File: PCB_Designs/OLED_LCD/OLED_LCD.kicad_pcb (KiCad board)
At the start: 2 copper layers, 25 parts, among them P1 CONN_01X10, P2 CONN_01X20, SW1 Rotary_Encoder_Switch, U1 MCP23017, U2 MCP23017, U3 CHERRY-MX

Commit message: s¨å
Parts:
- removed 0.1k1: 100, Resistors_SMD:R_0603_HandSoldering
- moved 100n3 88.0 mm to (178.8, 84.1)
- moved R4 72.7 mm to (116.6, 117.6)
- moved 10k8 65.3 mm to (139.2, 97.0), turned to 180 degrees
- moved 100n4 61.6 mm to (112.3, 106.4)
- moved 10k3 58.6 mm to (105.4, 87.1), turned to 90 degrees
- moved 10k1 57.5 mm to (100.3, 87.1)
- moved 10k2 53.8 mm to (113.3, 95.5)
- moved R2 53.1 mm to (102.6, 127.5)
- moved R1 50.1 mm to (112.0, 117.6), turned to 180 degrees
- moved 100n2 47.5 mm to (119.4, 91.4), turned to 180 degrees
- moved C1 45.3 mm to (112.0, 120.1), turned to 180 degrees
- moved 10k4 42.7 mm to (113.3, 91.4), turned to 180 degrees
- moved P1 41.0 mm to (129.3, 135.9)
- moved 10k7 40.9 mm to (137.7, 108.7), turned to 90 degrees
- moved R3 40.7 mm to (112.0, 115.1)
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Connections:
- P2 pad 19: /LED+ -> /LCD_BACKLIGHT
- U1 pad 18: /RST# -> Net-(U1-Pad18)
- U2 pad 18: /RST# -> Net-(U2-Pad18)
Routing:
- net /VCC5: track 0.00 -> 363.4 mm, vias 0 -> 2
- net GND: track 0.00 -> 215.9 mm, vias 0 -> 14
- net /LCD_BACKLIGHT: track 0.00 -> 76.9 mm, vias 0 -> 4
- net /CS2: track 0.00 -> 72.5 mm
- net /SCL#: track 0.00 -> 63.1 mm
- net /V0: track 0.00 -> 62.2 mm
- net /RS: track 0.00 -> 61.9 mm
- net /RST: track 0.00 -> 59.9 mm, vias 0 -> 2
- net /RW: track 0.00 -> 57.3 mm
- net /E: track 0.33 -> 53.1 mm
- net /SDA#: track 0.15 -> 50.5 mm
- net /INTA: track 0.00 -> 30.1 mm
- net /ENCODERA: track 0.00 -> 27.6 mm
- net /D0: track 0.00 -> 25.0 mm
- net /D1: track 0.00 -> 24.5 mm
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- added copper zone on F.Cu, net GND
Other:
- net class Default: clearance 0.6 -> 0.5
- rule trace_clearance: 0.6 -> 0.5

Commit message: LCD123
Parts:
- P1: footprint Connectors:IDC_Header_Straight_10pins -> Connectors_Multicomp:Multicomp_MC9A22-1034_2x05x2.54mm_Angled; moved to B.Cu
- moved P1 30.9 mm to (98.6, 133.1), turned to 0 degrees
- moved 100n2 1.60 mm to (117.8, 91.4)
- moved 100n1 1.44 mm to (113.3, 97.4)
- moved 10k5 0.74 mm to (112.3, 104.6)
- moved C1 0.71 mm to (112.0, 119.4)
- moved R3 0.66 mm to (112.0, 115.7)
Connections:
- net /INTB renamed Net-(U1-Pad19)
- P1 pad 10: Net-(P1-Pad10) -> /INTA
- P1 pad 4: Net-(P1-Pad4) -> GND
- P1 pad 6: Net-(P1-Pad6) -> /SDA#
- P1 pad 8: Net-(P1-Pad8) -> /SCL#
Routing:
- net /VCC5: track 363.4 -> 281.7 mm, vias 2 -> 4
- net /SDA#: track 50.5 -> 72.6 mm
- net /LCD_BACKLIGHT: track 76.9 -> 94.4 mm, vias 4 -> 2
- net /SCL#: track 63.1 -> 79.5 mm
- net GND: track 215.9 -> 201.1 mm, vias 14 -> 10
- net /INTA: track 30.1 -> 37.7 mm
- net Net-(C1-Pad1): track 7.51 -> 6.14 mm
- net /ENCODERA: track 27.6 -> 26.6 mm
- net Net-(10k1-Pad2): track 17.9 -> 17.0 mm
- net /ENCODERSW: track 24.5 -> 23.7 mm
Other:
- board text added: "Sunshine"

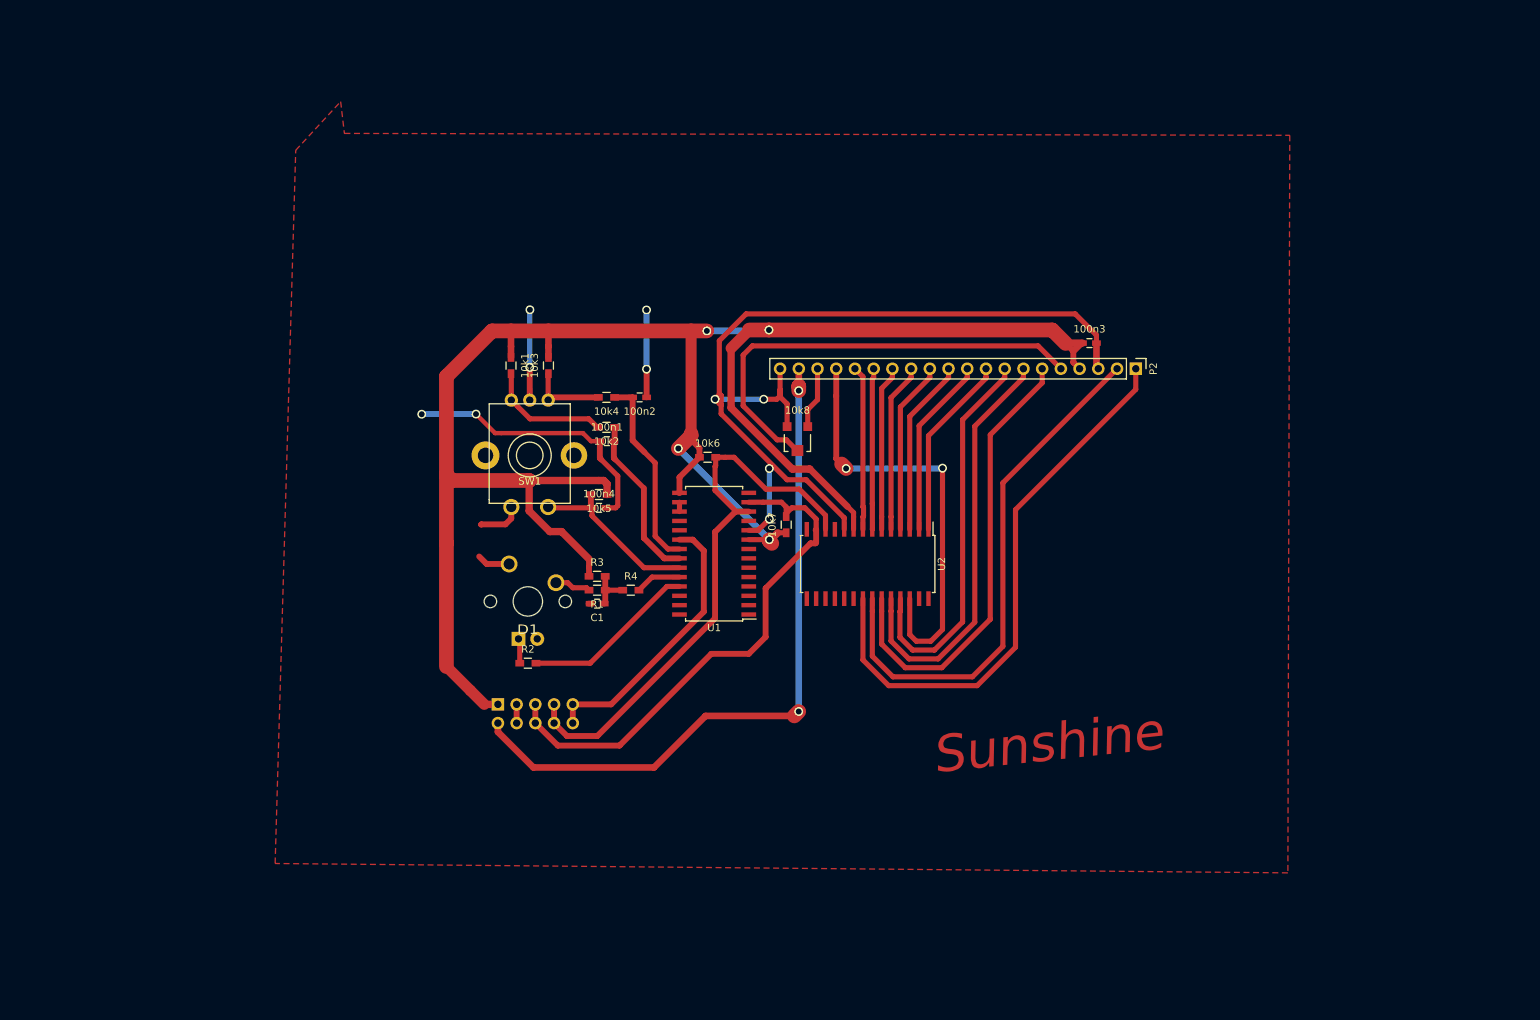
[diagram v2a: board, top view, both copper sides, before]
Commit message: Completed OLED_LCD_PCB v1.1
* Added Mountingholes.
* Added "Fatpads" for vias (were on some but not all earlier)
* Added bottom ground (Or etching will be a bitch)
* Added Edge cuts (105x65mm)
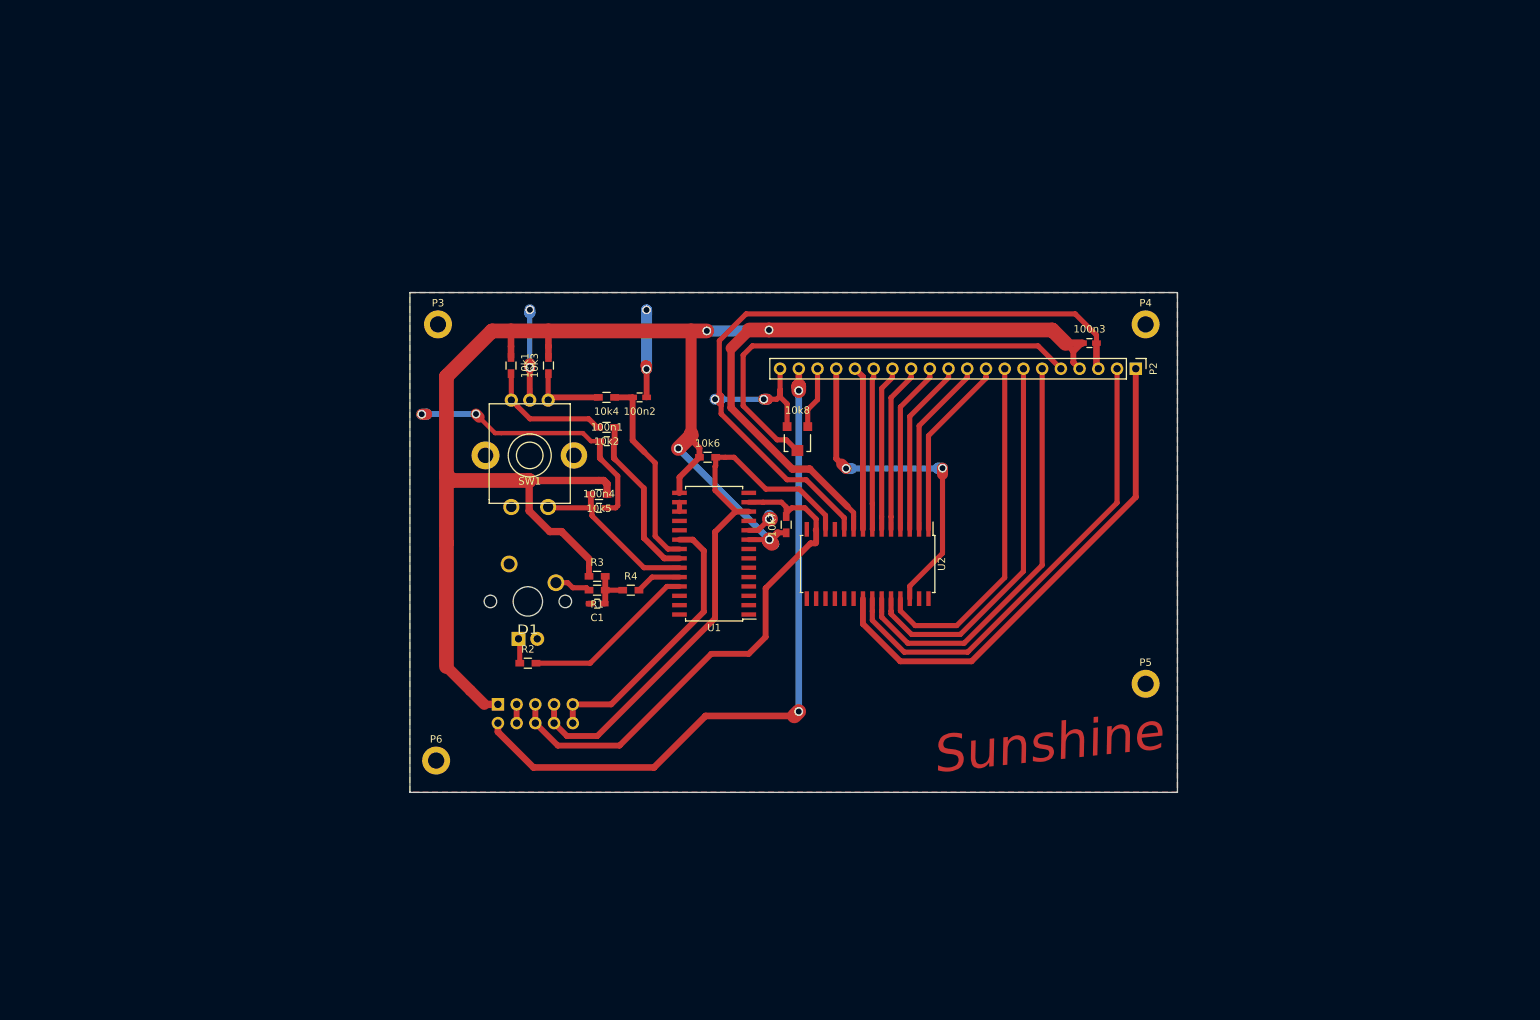
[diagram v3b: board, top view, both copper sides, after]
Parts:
- added P3: CONN_01X01, Mounting_Holes:MountingHole_2.2mm_M2_DIN965_Pad, F.Cu at (90.4, 81.5)
- added P4: CONN_01X01, Mounting_Holes:MountingHole_2.2mm_M2_DIN965_Pad, F.Cu at (186.4, 81.5)
- added P5: CONN_01X01, Mounting_Holes:MountingHole_2.2mm_M2_DIN965_Pad, F.Cu at (186.4, 130.3)
- added P6: CONN_01X01, Mounting_Holes:MountingHole_2.2mm_M2_DIN965_Pad, F.Cu at (90.2, 140.7)
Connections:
- U1 pad 1: Net-(U1-Pad1) -> (no net)
- U1 pad 18: Net-(U1-Pad18) -> (no net)
- U1 pad 19: Net-(U1-Pad19) -> (no net)
- U1 pad 2: Net-(U1-Pad2) -> (no net)
- U1 pad 26: Net-(U1-Pad26) -> (no net)
- U1 pad 27: Net-(U1-Pad27) -> (no net)
- U1 pad 28: Net-(U1-Pad28) -> (no net)
- U1 pad 3: Net-(U1-Pad3) -> (no net)
- U1 pad 4: Net-(U1-Pad4) -> (no net)
- U1 pad 5: Net-(U1-Pad5) -> (no net)
- U1 pad 6: Net-(U1-Pad6) -> (no net)
- U1 pad 7: Net-(U1-Pad7) -> (no net)
- U1 pad 8: Net-(U1-Pad8) -> (no net)
- U2 pad 18: Net-(U2-Pad18) -> (no net)
- U2 pad 19: Net-(U2-Pad19) -> (no net)
- U2 pad 20: Net-(U2-Pad20) -> (no net)
- U2 pad 27: Net-(U2-Pad27) -> (no net)
- U2 pad 28: Net-(U2-Pad28) -> (no net)
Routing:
- net /RST: track 59.5 -> 48.2 mm
- net GND: track 201.1 -> 191.6 mm, vias 10 -> 9
- net /CS1: track 77.2 -> 69.2 mm
- net /CS2: track 72.5 -> 64.5 mm
- net /E: track 53.1 -> 48.0 mm
- net /RS: track 61.9 -> 56.8 mm
- net /RW: track 57.3 -> 52.2 mm
- net /VCC5: track 281.7 -> 283.3 mm
- net /LCD_BACKLIGHT: track 94.4 -> 95.0 mm
- added copper zone on B.Cu, net GND
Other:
- board outline added: 104.1 x 67.8 mm

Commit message: hej
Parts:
- removed 10k8: 10k, Potentiometers:Potentiometer_Trimmer-EVM3E
- P2: value CONN_01X20 -> CONN_01X16; footprint Pin_Headers:Pin_Header_Straight_1x20_Pitch2.54mm -> Pin_Headers:Pin_Header_Straight_1x16_Pitch2.54mm
- moved 100n3 2.03 mm to (180.8, 83.5)
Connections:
- P2 pad 1: /CS1 -> GND
- P2 pad 10: /D1 -> /D3
- P2 pad 11: /D2 -> /D4
- P2 pad 12: /D3 -> /D5
- P2 pad 13: /D4 -> /D6
- P2 pad 14: /D5 -> /D7
- P2 pad 15: /D6 -> /LCD_BACKLIGHT
- P2 pad 16: /D7 -> GND
- P2 pad 2: /CS2 -> /VCC5
- P2 pad 3: GND -> Net-(P2-Pad3)
- P2 pad 4: /VCC5 -> /RS
- P2 pad 5: /V0 -> /RW
- P2 pad 6: /RS -> /E
- P2 pad 7: /RW -> /D0
- P2 pad 8: /E -> /D1
- P2 pad 9: /D0 -> /D2
- P3 pad 1: (no net) -> Net-(P3-Pad1)
- P4 pad 1: (no net) -> Net-(P4-Pad1)
- P5 pad 1: (no net) -> Net-(P5-Pad1)
- P6 pad 1: (no net) -> Net-(P6-Pad1)
- U1 pad 1: (no net) -> Net-(U1-Pad1)
- U1 pad 18: (no net) -> Net-(U1-Pad18)
- U1 pad 19: (no net) -> Net-(U1-Pad19)
- U1 pad 2: (no net) -> Net-(U1-Pad2)
- U1 pad 26: (no net) -> Net-(U1-Pad26)
- U1 pad 27: (no net) -> Net-(U1-Pad27)
- U1 pad 28: (no net) -> Net-(U1-Pad28)
- U1 pad 3: (no net) -> Net-(U1-Pad3)
- U1 pad 4: (no net) -> Net-(U1-Pad4)
- U1 pad 5: (no net) -> Net-(U1-Pad5)
- U1 pad 6: (no net) -> Net-(U1-Pad6)
- U1 pad 7: (no net) -> Net-(U1-Pad7)
- U1 pad 8: (no net) -> Net-(U1-Pad8)
- U2 pad 18: (no net) -> Net-(U2-Pad18)
- U2 pad 19: (no net) -> Net-(U2-Pad19)
- U2 pad 20: (no net) -> Net-(U2-Pad20)
- U2 pad 21: /CS1 -> Net-(U2-Pad21)
- U2 pad 22: /CS2 -> Net-(U2-Pad22)
- U2 pad 26: /RST -> Net-(U2-Pad26)
- U2 pad 27: (no net) -> Net-(U2-Pad27)
- U2 pad 28: (no net) -> Net-(U2-Pad28)
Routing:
- net /CS1: track 69.2 -> 0.00 mm
- net /CS2: track 64.5 -> 0.00 mm
- net /V0: track 61.7 -> 0.00 mm
- net /RST: track 48.2 -> 0.00 mm, vias 2 -> 0
- net /VEE: track 8.40 -> 0.00 mm
- net /VCC5: track 283.3 -> 288.5 mm, vias 4 -> 2
- net /D1: track 24.5 -> 26.9 mm
- net /D6: track 21.9 -> 24.0 mm
- net /D5: track 22.4 -> 24.5 mm
- net /D4: track 22.9 -> 25.0 mm
- net /D2: track 24.0 -> 26.1 mm
- net /D3: track 23.5 -> 25.6 mm
- net /D0: track 25.0 -> 27.1 mm
- net /LCD_BACKLIGHT: track 95.0 -> 93.2 mm
- net /E: track 48.0 -> 46.5 mm
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
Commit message: stuff
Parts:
- moved P5 10.6 mm to (186.4, 140.9)
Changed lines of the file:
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@@
-(kicad_pcb (version 4) (host pcbnew 4.0.5)
+(kicad_pcb (version 4) (host pcbnew 4.0.4-stable)
   (general
     (links 70)
@@
   )
   (setup
-    (last_trace_width 1.5)
+    (last_trace_width 0.8)
     (user_trace_width 0.6)
     (user_trace_width 0.7)
@@
   )
   (module Mounting_Holes:MountingHole_2.2mm_M2_DIN965_Pad (layer F.Cu)
-    (at 186.436 130.302)
+    (at 186.42 140.92)
     (descr "Mounting Hole 2.2mm, M2, DIN965")
     (tags "mounting hole 2.2mm m2 din965")

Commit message: LCD Reset -> 5V
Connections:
- U1 pad 18: Net-(U1-Pad18) -> /VCC5
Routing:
- net /VCC5: track 288.5 -> 297.7 mm
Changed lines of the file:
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@@
 (kicad_pcb (version 4) (host pcbnew 4.0.4-stable)
   (general
-    (links 70)
-    (no_connects 0)
-    (area 68.62 64.305136 212.368541 149.471)
+    (links 71)
+    (no_connects 1)
+    (area 86.538999 77.140999 190.829001 145.109001)
     (thickness 1.6)
     (drawings 10)
-    (tracks 310)
+    (tracks 315)
     (zones 0)
     (modules 27)
-    (nets 54)
+    (nets 53)
   )
   (page A4)
@@
   (net 39 "Net-(U1-Pad7)")
   (net 40 "Net-(U1-Pad8)")
-  (net 41 "Net-(U1-Pad18)")
-  (net 42 "Net-(U1-Pad19)")
-  (net 43 "Net-(U1-Pad26)")
-  (net 44 "Net-(U1-Pad27)")
-  (net 45 "Net-(U1-Pad28)")
-  (net 46 "Net-(U2-Pad18)")
-  (net 47 "Net-(U2-Pad19)")
-  (net 48 "Net-(U2-Pad20)")
-  (net 49 "Net-(U2-Pad21)")
-  (net 50 "Net-(U2-Pad22)")
-  (net 51 "Net-(U2-Pad26)")
-  (net 52 "Net-(U2-Pad27)")
-  (net 53 "Net-(U2-Pad28)")
+  (net 41 "Net-(U1-Pad19)")
+  (net 42 "Net-(U1-Pad26)")
+  (net 43 "Net-(U1-Pad27)")
+  (net 44 "Net-(U1-Pad28)")
+  (net 45 "Net-(U2-Pad18)")
+  (net 46 "Net-(U2-Pad19)")
+  (net 47 "Net-(U2-Pad20)")
+  (net 48 "Net-(U2-Pad21)")
+  (net 49 "Net-(U2-Pad22)")
+  (net 50 "Net-(U2-Pad26)")
+  (net 51 "Net-(U2-Pad27)")
+  (net 52 "Net-(U2-Pad28)")
   (net_class Default "This is the default net class."
     (clearance 0.5)
@@
     (add_net "Net-(R1-Pad2)")
     (add_net "Net-(U1-Pad1)")
-    (add_net "Net-(U1-Pad18)")
     (add_net "Net-(U1-Pad19)")
     (add_net "Net-(U1-Pad2)")
@@
       (net 9 GND))
     (pad 18 smd rect (at 4.7 4.445 270) (size 2 0.6) (layers F.Cu F.Paste F.Mask)
-      (net 46 "Net-(U2-Pad18)"))
+      (net 45 "Net-(U2-Pad18)"))
     (pad 19 smd rect (at 4.7 3.175 270) (size 2 0.6) (layers F.Cu F.Paste F.Mask)
-      (net 47 "Net-(U2-Pad19)"))
+      (net 46 "Net-(U2-Pad19)"))
     (pad 20 smd rect (at 4.7 1.905 270) (size 2 0.6) (layers F.Cu F.Paste F.Mask)
-      (net 48 "Net-(U2-Pad20)"))
+      (net 47 "Net-(U2-Pad20)"))
     (pad 21 smd rect (at 4.7 0.635 270) (size 2 0.6) (layers F.Cu F.Paste F.Mask)
-      (net 49 "Net-(U2-Pad21)"))
+      (net 48 "Net-(U2-Pad21)"))
     (pad 22 smd rect (at 4.7 -0.635 270) (size 2 0.6) (layers F.Cu F.Paste F.Mask)
-      (net 50 "Net-(U2-Pad22)"))
+      (net 49 "Net-(U2-Pad22)"))
     (pad 23 smd rect (at 4.7 -1.905 270) (size 2 0.6) (layers F.Cu F.Paste F.Mask)
       (net 10 /RS))
@@
       (net 12 /E))
     (pad 26 smd rect (at 4.7 -5.715 270) (size 2 0.6) (layers F.Cu F.Paste F.Mask)
-      (net 51 "Net-(U2-Pad26)"))
+      (net 50 "Net-(U2-Pad26)"))
     (pad 27 smd rect (at 4.7 -6.985 270) (size 2 0.6) (layers F.Cu F.Paste F.Mask)
-      (net 52 "Net-(U2-Pad27)"))
+      (net 51 "Net-(U2-Pad27)"))
     (pad 28 smd rect (at 4.7 -8.255 270) (size 2 0.6) (layers F.Cu F.Paste F.Mask)
-      (net 53 "Net-(U2-Pad28)"))
+      (net 52 "Net-(U2-Pad28)"))
     (model Housings_SOIC.3dshapes/SOIC-28_7.5x17.9mm_Pitch1.27mm.wrl
       (at (xyz 0 0 0))
@@
       (net 9 GND))
     (pad 18 smd rect (at 4.7 4.445 180) (size 2 0.6) (layers F.Cu F.Paste F.Mask)
-      (net 41 "Net-(U1-Pad18)"))
+      (net 1 /VCC5))
     (pad 19 smd rect (at 4.7 3.175 180) (size 2 0.6) (layers F.Cu F.Paste F.Mask)
-      (net 42 "Net-(U1-Pad19)"))
+      (net 41 "Net-(U1-Pad19)"))
     (pad 20 smd rect (at 4.7 1.905 180) (size 2 0.6) (layers F.Cu F.Paste F.Mask)
       (net 21 /INTA))
@@
       (net 26 /BUTT_LED))
     (pad 26 smd rect (at 4.7 -5.715 180) (size 2 0.6) (layers F.Cu F.Paste F.Mask)
-      (net 43 "Net-(U1-Pad26)"))
+      (net 42 "Net-(U1-Pad26)"))
     (pad 27 smd rect (at 4.7 -6.985 180) (size 2 0.6) (layers F.Cu F.Paste F.Mask)
-      (net 44 "Net-(U1-Pad27)"))
+      (net 43 "Net-(U1-Pad27)"))
     (pad 28 smd rect (at 4.7 -8.255 180) (size 2 0.6) (layers F.Cu F.Paste F.Mask)
-      (net 45 "Net-(U1-Pad28)"))
+      (net 44 "Net-(U1-Pad28)"))
     (model Housings_SOIC.3dshapes/SOIC-28_7.5x17.9mm_Pitch1.27mm.wrl
       (at (xyz 0 0 0))
@@
     (arrow2b (pts (xy 86.613633 67.005136) (xy 87.740137 66.418715)))
   )
+  (segment (start 123.188 108.204) (end 125.634 108.204) (width 0.8) (layer F.Cu) (net 1))
+  (segment (start 125.634 108.204) (end 126.3 107.538) (width 0.8) (layer F.Cu) (net 1))
+  (segment (start 126.3 107.538) (end 126.3 105.13) (width 0.8) (layer F.Cu) (net 1))
+  (segment (start 126.3 105.13) (end 125.564 104.394) (width 0.8) (layer F.Cu) (net 1))
+  (segment (start 125.564 104.394) (end 123.188 104.394) (width 0.8) (layer F.Cu) (net 1))
   (segment (start 182.559319 87.551401) (end 179.8218 84.813882) (width 0.8) (layer F.Cu) (net 1))
   (segment (start 179.8218 84.813882) (end 179.8218 83.5406) (width 0.8) (layer F.Cu) (net 1))
